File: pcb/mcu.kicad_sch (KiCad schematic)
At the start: 19 parts, among them J3 Conn_02x03_Counter_Clockwise, J4 Conn_01x06, J5 Conn_01x06, SW6 SW_Push, U3 STM32F042K6Tx, U4 TLV70033_SOT23-5

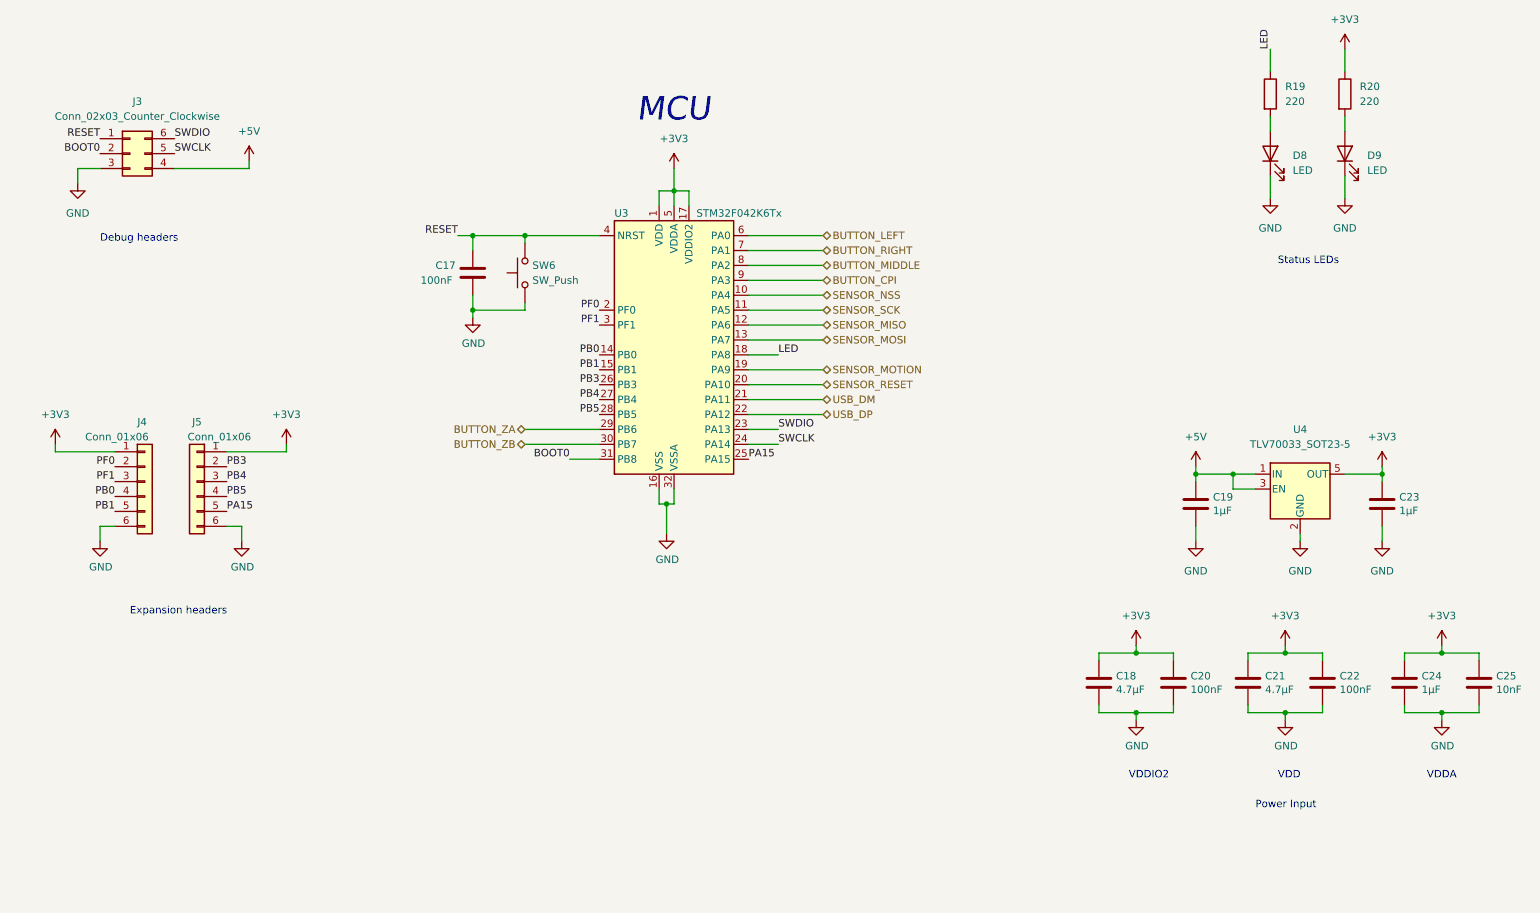
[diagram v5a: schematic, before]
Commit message: - added boot select resistor - regenerated netlist - adjusted pcb component placement
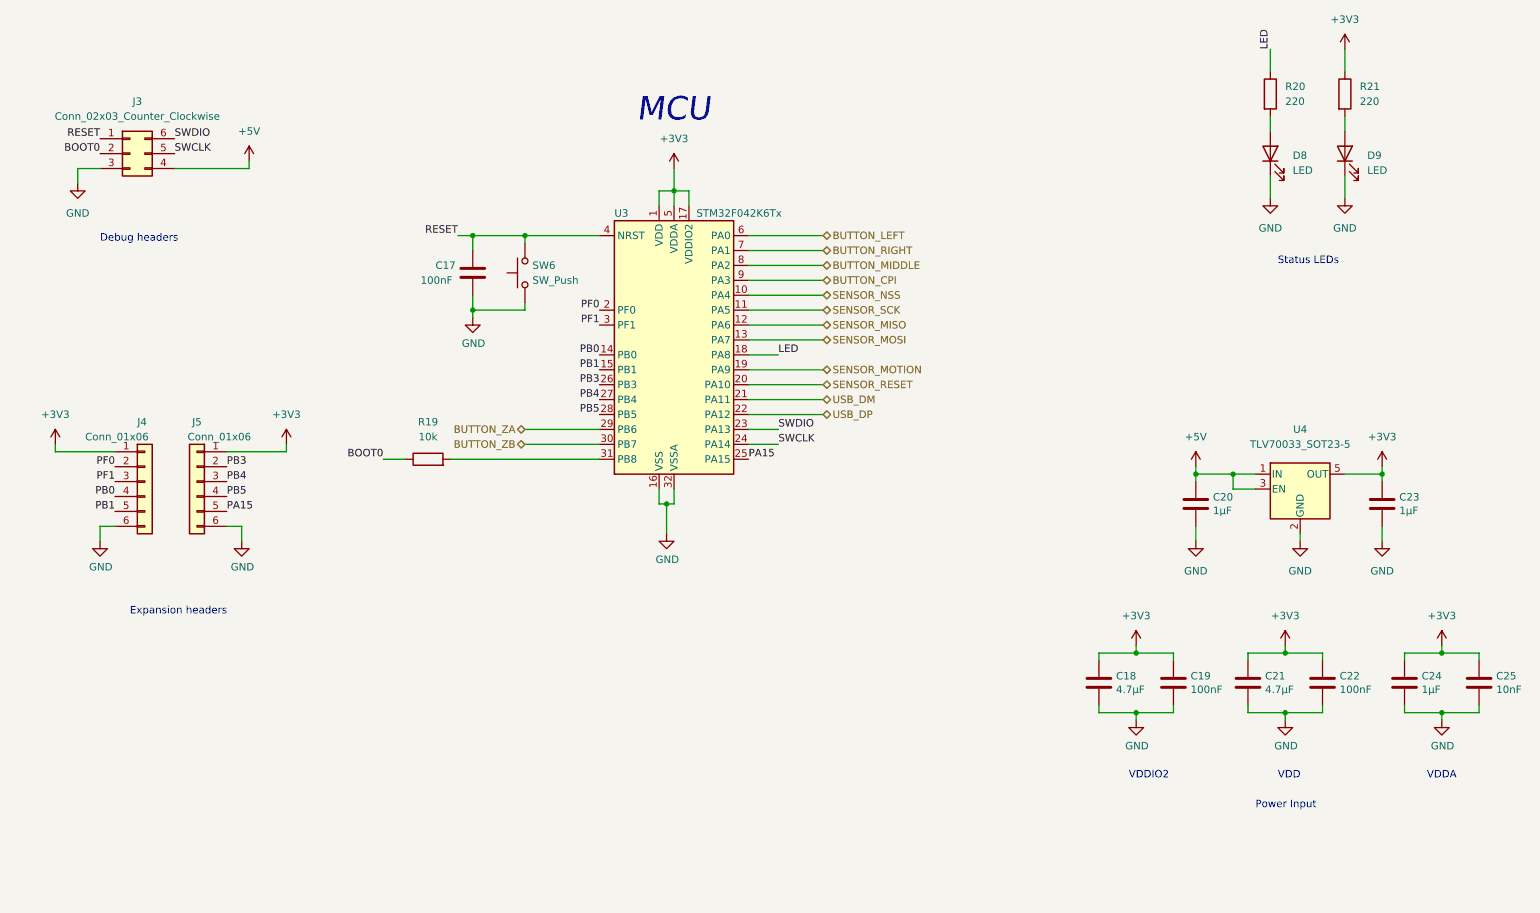
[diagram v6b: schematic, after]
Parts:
- added R19: 10k, Resistor_SMD:R_0603_1608Metric, symbol Device:R
- renumbered C20 to C19, C19 to C20, R19 to R20, R20 to R21
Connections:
- net BOOT0: now also R19.1; no longer U3.31 (PB8)
- new net: R19.2, U3.31 (PB8)
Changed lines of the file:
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@@
     (stroke (width 0) (type default) (color 0 0 0 0))
   )
-  (wire (pts (xy 113.03 101.6) (xy 118.11 101.6))
+  (wire (pts (xy 81.28 101.6) (xy 85.09 101.6))
     (stroke (width 0) (type default) (color 0 0 0 0))
   )
@@
   )
   (wire (pts (xy 128.27 55.88) (xy 130.81 55.88))
+    (stroke (width 0) (type default) (color 0 0 0 0))
+  )
+  (wire (pts (xy 92.71 101.6) (xy 118.11 101.6))
     (stroke (width 0) (type default) (color 0 0 0 0))
   )
@@
     (effects (font (size 1.27 1.27)) (justify right bottom))
   )
-  (label "BOOT0" (at 113.03 101.6 180)
+  (label "BOOT0" (at 81.28 101.6 180)
     (effects (font (size 1.27 1.27)) (justify right bottom))
   )
@@
   (symbol (lib_id "power:GND") (at 237.49 115.57 0) (unit 1)
     (in_bom yes) (on_board yes) (fields_autoplaced)
-    (property "Reference" "#PWR049" (id 0) (at 237.49 121.92 0)
+    (property "Reference" "#PWR052" (id 0) (at 237.49 121.92 0)
       (effects (font (size 1.27 1.27)) hide)
     )
@@
   (symbol (lib_id "power:GND") (at 219.71 115.57 0) (unit 1)
     (in_bom yes) (on_board yes) (fields_autoplaced)
-    (property "Reference" "#PWR047" (id 0) (at 219.71 121.92 0)
+    (property "Reference" "#PWR048" (id 0) (at 219.71 121.92 0)
       (effects (font (size 1.27 1.27)) hide)
     )
@@
   (symbol (lib_id "power:GND") (at 209.55 146.05 0) (unit 1)
     (in_bom yes) (on_board yes)
-    (property "Reference" "#PWR045" (id 0) (at 209.55 152.4 0)
+    (property "Reference" "#PWR046" (id 0) (at 209.55 152.4 0)
       (effects (font (size 1.27 1.27)) hide)
     )
@@
   (symbol (lib_id "power:+3V3") (at 130.81 52.07 0) (unit 1)
     (in_bom yes) (on_board yes) (fields_autoplaced)
-    (property "Reference" "#PWR043" (id 0) (at 130.81 55.88 0)
+    (property "Reference" "#PWR044" (id 0) (at 130.81 55.88 0)
       (effects (font (size 1.27 1.27)) hide)
     )
@@
   (symbol (lib_id "power:+3V3") (at 64.77 99.06 0) (unit 1)
     (in_bom yes) (on_board yes) (fields_autoplaced)
-    (property "Reference" "#PWR040" (id 0) (at 64.77 102.87 0)
+    (property "Reference" "#PWR041" (id 0) (at 64.77 102.87 0)
       (effects (font (size 1.27 1.27)) hide)
     )
@@
   (symbol (lib_id "power:+3V3") (at 209.55 133.35 0) (unit 1)
     (in_bom yes) (on_board yes) (fields_autoplaced)
-    (property "Reference" "#PWR044" (id 0) (at 209.55 137.16 0)
+    (property "Reference" "#PWR045" (id 0) (at 209.55 137.16 0)
       (effects (font (size 1.27 1.27)) hide)
     )
@@
   (symbol (lib_id "power:+3V3") (at 245.11 31.75 0) (unit 1)
     (in_bom yes) (on_board yes) (fields_autoplaced)
-    (property "Reference" "#PWR052" (id 0) (at 245.11 35.56 0)
+    (property "Reference" "#PWR053" (id 0) (at 245.11 35.56 0)
       (effects (font (size 1.27 1.27)) hide)
     )
@@
   (symbol (lib_id "power:+3V3") (at 251.46 102.87 0) (unit 1)
     (in_bom yes) (on_board yes) (fields_autoplaced)
-    (property "Reference" "#PWR054" (id 0) (at 251.46 106.68 0)
+    (property "Reference" "#PWR055" (id 0) (at 251.46 106.68 0)
       (effects (font (size 1.27 1.27)) hide)
     )
@@
   (symbol (lib_id "power:GND") (at 232.41 57.15 0) (unit 1)
     (in_bom yes) (on_board yes) (fields_autoplaced)
-    (property "Reference" "#PWR048" (id 0) (at 232.41 63.5 0)
+    (property "Reference" "#PWR049" (id 0) (at 232.41 63.5 0)
       (effects (font (size 1.27 1.27)) hide)
     )
@@
   (symbol (lib_id "power:GND") (at 96.52 77.47 0) (unit 1)
     (in_bom yes) (on_board yes)
-    (property "Reference" "#PWR041" (id 0) (at 96.52 83.82 0)
+    (property "Reference" "#PWR042" (id 0) (at 96.52 83.82 0)
       (effects (font (size 1.27 1.27)) hide)
     )
@@
   (symbol (lib_id "power:+3V3") (at 261.62 133.35 0) (unit 1)
     (in_bom yes) (on_board yes) (fields_autoplaced)
-    (property "Reference" "#PWR056" (id 0) (at 261.62 137.16 0)
+    (property "Reference" "#PWR057" (id 0) (at 261.62 137.16 0)
       (effects (font (size 1.27 1.27)) hide)
     )
@@
   (symbol (lib_id "power:GND") (at 251.46 115.57 0) (unit 1)
     (in_bom yes) (on_board yes) (fields_autoplaced)
-    (property "Reference" "#PWR055" (id 0) (at 251.46 121.92 0)
+    (property "Reference" "#PWR056" (id 0) (at 251.46 121.92 0)
       (effects (font (size 1.27 1.27)) hide)
     )
@@
   (symbol (lib_id "power:+3V3") (at 25.4 99.06 0) (unit 1)
     (in_bom yes) (on_board yes) (fields_autoplaced)
-    (property "Reference" "#PWR035" (id 0) (at 25.4 102.87 0)
+    (property "Reference" "#PWR036" (id 0) (at 25.4 102.87 0)
       (effects (font (size 1.27 1.27)) hide)
     )
@@
   (symbol (lib_id "power:GND") (at 33.02 115.57 0) (unit 1)
     (in_bom yes) (on_board yes)
-    (property "Reference" "#PWR037" (id 0) (at 33.02 121.92 0)
+    (property "Reference" "#PWR038" (id 0) (at 33.02 121.92 0)
       (effects (font (size 1.27 1.27)) hide)
     )
@@
     (pin "1")
   )
+  (symbol (lib_id "Device:R") (at 88.9 101.6 90) (unit 1)
+    (in_bom yes) (on_board yes) (fields_autoplaced)
+    (property "Reference" "R19" (id 0) (at 88.9 95.25 90))
+    (property "Value" "10k" (id 1) (at 88.9 97.79 90))
+    (property "Footprint" "Resistor_SMD:R_0603_1608Metric" (id 2) (at 88.9 103.378 90)
+      (effects (font (size 1.27 1.27)) hide)
+    )
+    (property "Datasheet" "~" (id 3) (at 88.9 101.6 0)
+      (effects (font (size 1.27 1.27)) hide)
+    )
+    (property "LCSC" "C25804" (id 4) (at 88.9 101.6 0)
+      (effects (font (size 1.27 1.27)) hide)
+    )
+    (pin "1")
+    (pin "2")
+  )
   (symbol (lib_id "power:GND") (at 57.15 115.57 0) (unit 1)
     (in_bom yes) (on_board yes)
-    (property "Reference" "#PWR038" (id 0) (at 57.15 121.92 0)
+    (property "Reference" "#PWR039" (id 0) (at 57.15 121.92 0)
       (effects (font (size 1.27 1.27)) hide)
     )
@@
   (symbol (lib_id "power:+5V") (at 219.71 102.87 0) (unit 1)
     (in_bom yes) (on_board yes) (fields_autoplaced)
-    (property "Reference" "#PWR046" (id 0) (at 219.71 106.68 0)
+    (property "Reference" "#PWR047" (id 0) (at 219.71 106.68 0)
       (effects (font (size 1.27 1.27)) hide)
     )
@@
   (symbol (lib_id "power:GND") (at 245.11 57.15 0) (unit 1)
     (in_bom yes) (on_board yes) (fields_autoplaced)
-    (property "Reference" "#PWR053" (id 0) (at 245.11 63.5 0)
+    (property "Reference" "#PWR054" (id 0) (at 245.11 63.5 0)
       (effects (font (size 1.27 1.27)) hide)
     )
@@
   (symbol (lib_id "power:+5V") (at 58.42 50.8 0) (unit 1)
     (in_bom yes) (on_board yes) (fields_autoplaced)
-    (property "Reference" "#PWR039" (id 0) (at 58.42 54.61 0)
+    (property "Reference" "#PWR040" (id 0) (at 58.42 54.61 0)
       (effects (font (size 1.27 1.27)) hide)
     )
@@
   (symbol (lib_id "Device:C") (at 215.9 139.7 0) (unit 1)
     (in_bom yes) (on_board yes)
-    (property "Reference" "C20" (id 0) (at 218.821 138.5316 0)
+    (property "Reference" "C19" (id 0) (at 218.821 138.5316 0)
       (effects (font (size 1.27 1.27)) (justify left))
     )
@@
   (symbol (lib_id "Device:C") (at 219.71 109.22 0) (unit 1)
     (in_bom yes) (on_board yes)
-    (property "Reference" "C19" (id 0) (at 222.631 108.0516 0)
+    (property "Reference" "C20" (id 0) (at 222.631 108.0516 0)
       (effects (font (size 1.27 1.27)) (justify left))
     )
@@
   (symbol (lib_id "Device:R") (at 245.11 39.37 0) (unit 1)
     (in_bom yes) (on_board yes) (fields_autoplaced)
-    (property "Reference" "R20" (id 0) (at 247.65 38.0999 0)
+    (property "Reference" "R21" (id 0) (at 247.65 38.0999 0)
       (effects (font (size 1.27 1.27)) (justify left))
     )
@@
   (symbol (lib_id "power:GND") (at 29.21 54.61 0) (unit 1)
     (in_bom yes) (on_board yes) (fields_autoplaced)
-    (property "Reference" "#PWR036" (id 0) (at 29.21 60.96 0)
+    (property "Reference" "#PWR037" (id 0) (at 29.21 60.96 0)
       (effects (font (size 1.27 1.27)) hide)
     )
@@
   (symbol (lib_id "power:GND") (at 129.54 114.3 0) (unit 1)
     (in_bom yes) (on_board yes)
-    (property "Reference" "#PWR042" (id 0) (at 129.54 120.65 0)
+    (property "Reference" "#PWR043" (id 0) (at 129.54 120.65 0)
       (effects (font (size 1.27 1.27)) hide)
     )
@@
   (symbol (lib_id "Device:R") (at 232.41 39.37 0) (unit 1)
     (in_bom yes) (on_board yes) (fields_autoplaced)
-    (property "Reference" "R19" (id 0) (at 234.95 38.0999 0)
+    (property "Reference" "R20" (id 0) (at 234.95 38.0999 0)
       (effects (font (size 1.27 1.27)) (justify left))
     )
@@
   (symbol (lib_id "power:GND") (at 261.62 146.05 0) (unit 1)
     (in_bom yes) (on_board yes)
-    (property "Reference" "#PWR057" (id 0) (at 261.62 152.4 0)
-      (effects (font (size 1.27 1.27)) hide)
-    )
+    (property "Reference" "#PWR058" (id 0) (at 261.62 152.4 0)
+      (effects (font (size 1.27 1.27)) hide)
+    )

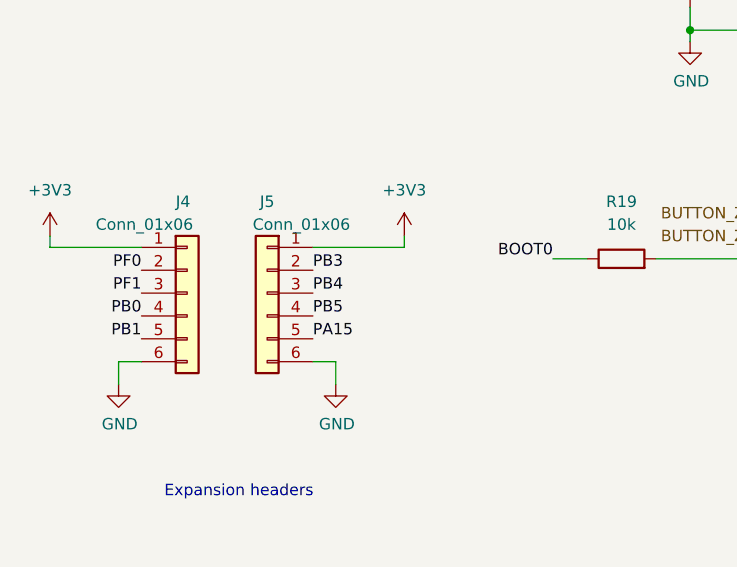
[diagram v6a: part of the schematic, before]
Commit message: connected all pcb elements with tracks
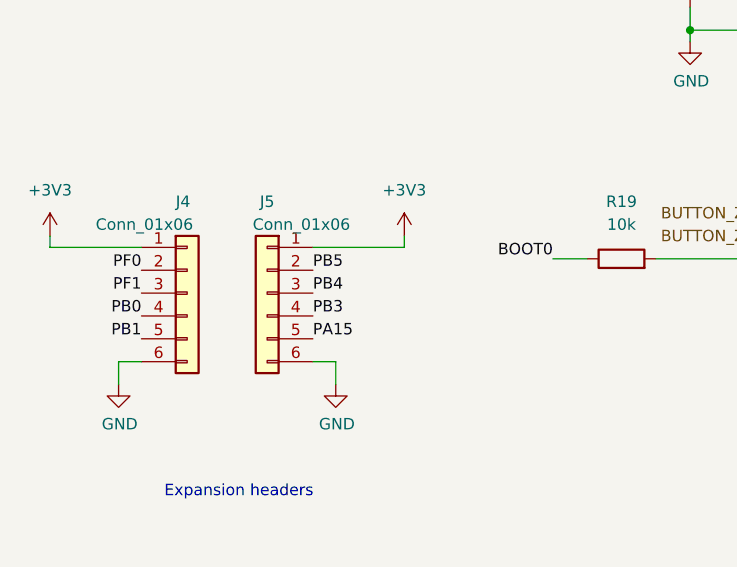
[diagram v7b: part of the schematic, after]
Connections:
- net PB3: now also J5.4 (Pin_4); no longer J5.2 (Pin_2)
- net PB5: now also J5.2 (Pin_2); no longer J5.4 (Pin_4)
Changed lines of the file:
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@@
     (effects (font (size 1.27 1.27)) (justify left bottom))
   )
-  (label "PB5" (at 54.61 107.95 0)
+  (label "PB3" (at 54.61 107.95 0)
     (effects (font (size 1.27 1.27)) (justify left bottom))
   )
@@
     (effects (font (size 1.27 1.27)) (justify right bottom))
   )
-  (label "PB3" (at 54.61 102.87 0)
+  (label "PB5" (at 54.61 102.87 0)
     (effects (font (size 1.27 1.27)) (justify left bottom))
   )

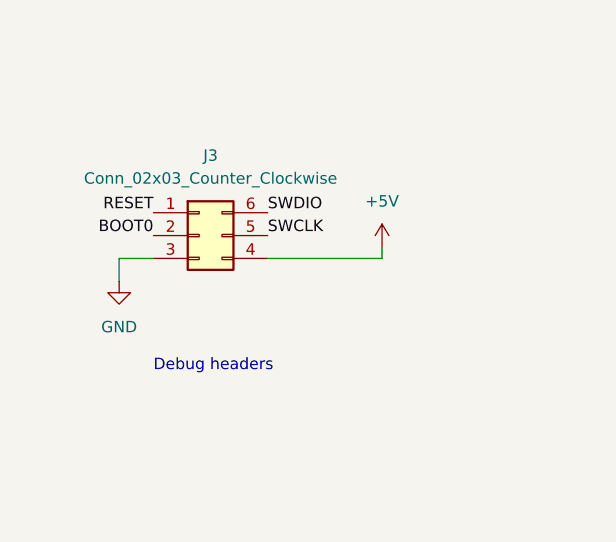
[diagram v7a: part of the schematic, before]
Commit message: manually connected GND on pcb
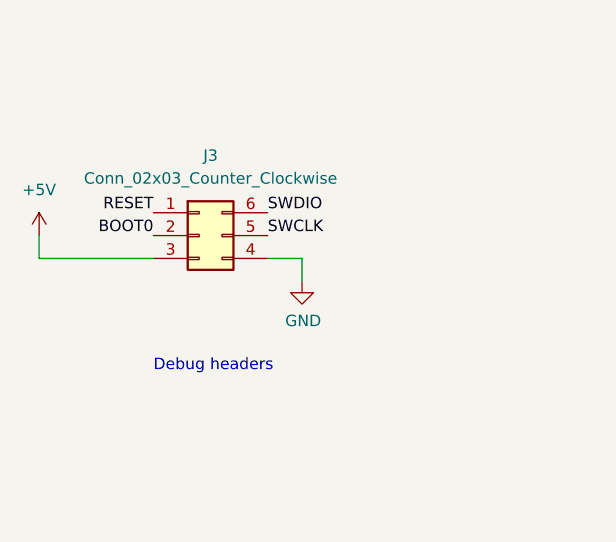
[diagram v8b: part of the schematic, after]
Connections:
- net +5V: now also J3.3 (Pin_3); no longer J3.4 (Pin_4)
- net GND: now also J3.4 (Pin_4); no longer J3.3 (Pin_3)
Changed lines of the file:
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@@
-    (stroke (width 0) (type default) (color 0 0 0 0))
-  )
-  (wire (pts (xy 29.21 52.07) (xy 29.21 54.61))
     (stroke (width 0) (type default) (color 0 0 0 0))
   )
@@
     (stroke (width 0) (type default) (color 0 0 0 0))
   )
-  (wire (pts (xy 58.42 50.8) (xy 58.42 52.07))
-    (stroke (width 0) (type default) (color 0 0 0 0))
-  )
   (wire (pts (xy 232.41 43.18) (xy 232.41 45.72))
     (stroke (width 0) (type default) (color 0 0 0 0))
@@
     (stroke (width 0) (type default) (color 0 0 0 0))
   )
-  (wire (pts (xy 58.42 52.07) (xy 45.72 52.07))
-    (stroke (width 0) (type default) (color 0 0 0 0))
-  )
   (wire (pts (xy 219.71 102.87) (xy 219.71 104.14))
     (stroke (width 0) (type default) (color 0 0 0 0))
   )
+  (wire (pts (xy 20.32 52.07) (xy 20.32 49.53))
+    (stroke (width 0) (type default) (color 0 0 0 0))
+  )
   (wire (pts (xy 130.81 58.42) (xy 130.81 55.88))
     (stroke (width 0) (type default) (color 0 0 0 0))
@@
     (stroke (width 0) (type default) (color 0 0 0 0))
   )
+  (wire (pts (xy 33.02 52.07) (xy 20.32 52.07))
+    (stroke (width 0) (type default) (color 0 0 0 0))
+  )
   (wire (pts (xy 226.06 106.68) (xy 226.06 104.14))
     (stroke (width 0) (type default) (color 0 0 0 0))
@@
     (stroke (width 0) (type default) (color 0 0 0 0))
   )
+  (wire (pts (xy 49.53 52.07) (xy 45.72 52.07))
+    (stroke (width 0) (type default) (color 0 0 0 0))
+  )
   (wire (pts (xy 156.21 66.04) (xy 143.51 66.04))
     (stroke (width 0) (type default) (color 0 0 0 0))
@@
     (stroke (width 0) (type default) (color 0 0 0 0))
   )
+  (wire (pts (xy 49.53 54.61) (xy 49.53 52.07))
+    (stroke (width 0) (type default) (color 0 0 0 0))
+  )
   (wire (pts (xy 130.81 55.88) (xy 133.35 55.88))
     (stroke (width 0) (type default) (color 0 0 0 0))
   )
   (wire (pts (xy 96.52 76.2) (xy 105.41 76.2))
-    (stroke (width 0) (type default) (color 0 0 0 0))
-  )
-  (wire (pts (xy 33.02 52.07) (xy 29.21 52.07))
     (stroke (width 0) (type default) (color 0 0 0 0))
   )
@@
     (pin "2")
   )
-  (symbol (lib_id "power:+5V") (at 58.42 50.8 0) (unit 1)
-    (in_bom yes) (on_board yes) (fields_autoplaced)
-    (property "Reference" "#PWR040" (id 0) (at 58.42 54.61 0)
-      (effects (font (size 1.27 1.27)) hide)
-    )
-    (property "Value" "+5V" (id 1) (at 58.42 45.72 0))
-    (property "Footprint" "" (id 2) (at 58.42 50.8 0)
-      (effects (font (size 1.27 1.27)) hide)
-    )
-    (property "Datasheet" "" (id 3) (at 58.42 50.8 0)
+  (symbol (lib_id "power:+5V") (at 20.32 49.53 0) (unit 1)
+    (in_bom yes) (on_board yes) (fields_autoplaced)
+    (property "Reference" "#PWR040" (id 0) (at 20.32 53.34 0)
+      (effects (font (size 1.27 1.27)) hide)
+    )
+    (property "Value" "+5V" (id 1) (at 20.32 44.45 0))
+    (property "Footprint" "" (id 2) (at 20.32 49.53 0)
+      (effects (font (size 1.27 1.27)) hide)
+    )
+    (property "Datasheet" "" (id 3) (at 20.32 49.53 0)
       (effects (font (size 1.27 1.27)) hide)
     )
@@
     (pin "1")
     (pin "2")
+  )
+  (symbol (lib_id "power:GND") (at 49.53 54.61 0) (unit 1)
+    (in_bom yes) (on_board yes)
+    (property "Reference" "#PWR?" (id 0) (at 49.53 60.96 0)
+      (effects (font (size 1.27 1.27)) hide)
+    )
+    (property "Value" "GND" (id 1) (at 49.657 59.0042 0))
+    (property "Footprint" "" (id 2) (at 49.53 54.61 0)
+      (effects (font (size 1.27 1.27)) hide)
+    )
+    (property "Datasheet" "" (id 3) (at 49.53 54.61 0)
+      (effects (font (size 1.27 1.27)) hide)
+    )
+    (pin "1")
   )
   (symbol (lib_id "Connector_Generic:Conn_01x06") (at 40.64 105.41 0) (unit 1)
@@
     (pin "6")
   )
-  (symbol (lib_id "power:GND") (at 29.21 54.61 0) (unit 1)
-    (in_bom yes) (on_board yes) (fields_autoplaced)
-    (property "Reference" "#PWR037" (id 0) (at 29.21 60.96 0)
-      (effects (font (size 1.27 1.27)) hide)
-    )
-    (property "Value" "GND" (id 1) (at 29.21 59.69 0))
-    (property "Footprint" "" (id 2) (at 29.21 54.61 0)
-      (effects (font (size 1.27 1.27)) hide)
-    )
-    (property "Datasheet" "" (id 3) (at 29.21 54.61 0)
-      (effects (font (size 1.27 1.27)) hide)
-    )
-    (pin "1")
-  )
   (symbol (lib_id "power:GND") (at 129.54 114.3 0) (unit 1)
